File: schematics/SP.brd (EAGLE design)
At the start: 72.1 x 32 mm, 35 parts

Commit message: Поправлены платы МК, Радио, Гермо
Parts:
- removed BME280: BME280BME280-PINS-ONLY, UNKNOWN-2024:BME280-PINS-ONLY
- removed C2, C3, C4: 100nF, rcl:C0603
- removed JP2: (no value), pinhead:1X02
- removed MICS-5524: MICS_5524, UNKNOWN-2024:MICS-5524
- removed MICS-6814: MICS-6814, CanCubeSat:MICS-6814
- removed R11, R12, R13, R8: 10k, rcl:R0603
- removed R16, R17, R2: 5k1, rcl:R0603
- removed R39, R41, R43, R45: 100k, rcl:R0603
- removed R40, R42, R44, R46: 1M, rcl:R0603
- removed U$10, U$11, U$12, U$9: CONNECT_3, UNKNOWN-2024:CONNECT_3
- removed U$14: AD5593, UNKNOWN-2024:AD5593
- added C1: 47u, rcl:C1210
- added D1, D2, D3, D4, D5, D6, D7: MBR0520LT, diode:SOD123
- added FOTO: VT93N1VERT, KNPN-2023:VT93N1-VERT
- added PWR: (no value), led:CHIP-LED0603
- added SP-OUT: (no value), pinhead:1X02
- added U$1, U$3: SOLAR-2_1, KNPN-2023:SOLAR_1-2
- JP1: device pinhead:1X04 -> pinhead:1X02
- R1: value 5k1 -> 2k7
- U$2: value Плата ГЕРМО -> SOLAR-2_0; device UNKNOWN-2024:LOGO -> KNPN-2023:SOLAR_0-2
- U$4: value CCS811 -> SOLAR-2_0; device UNKNOWN-2024:CSS811 -> KNPN-2023:SOLAR_0-2
- U$5: value CONNECT_3 -> Плата СП; device UNKNOWN-2024:CONNECT_3 -> UNKNOWN-2024:LOGO
- U$6: value CONNECT_3 -> SOLAR-2_0; device UNKNOWN-2024:CONNECT_3 -> KNPN-2023:SOLAR_0-2
- U$7: value CONNECT_3 -> (none); device UNKNOWN-2024:CONNECT_3 -> KNPN-2023:VIAS-CONNECT
- U$8: value CONNECT_3 -> SOLAR-2_1; device UNKNOWN-2024:CONNECT_3 -> KNPN-2023:SOLAR_1-2
- moved U$6 71.4 mm to (8.00, -14.5), turned to 0 degrees
- moved U$8 70.9 mm to (7.50, -28.5), turned to 0 degrees
- moved U$5 69.6 mm to (0.00, -4.00)
- moved U$7 39.5 mm to (15.0, 4.20)
- moved JP1 37.2 mm to (15.0, 43.5), turned to 180 degrees
- moved U$2 16.8 mm to (7.20, 13.5), turned to 270 degrees
- moved R1 14.1 mm to (19.1, 38.1), flipped to the bottom, turned to 180 degrees
- moved U$4 5.01 mm to (22.8, 32.5), flipped to the top, turned to 90 degrees
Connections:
- removed net 3V3: C3.1, C4.1, R2.2, R40.1, R42.1, R44.1, R46.1, U$10.1, U$11.1, U$12.1, U$14.P$3, U$14.P$9, U$5.1, U$6.1, U$7.1, U$8.1, U$9.1
- removed net 5V: BME280.P$4, JP1.2, MICS-5524.P$4, MICS-6814.P$1, U$4.P$1
- removed net CO: MICS-6814.P$5, R8.2, U$14.P$7
- removed net EN: MICS-5524.P$1, R17.1
- removed net FOTO0: JP2.2, U$14.P$5
- removed net FOTO1: JP2.1, U$14.P$4
- removed net GND: BME280.P$3, C2.2, C3.2, C4.2, JP1.1, MICS-5524.P$3, MICS-6814.P$2, R1.2, R16.2, R17.2, U$14.P$14, U$4.P$2
- removed net MICS: MICS-5524.P$2, R13.2, U$14.P$11
- removed net N$10: R12.1, U$9.2
- removed net N$11: R44.2, U$10.3
- removed net N$12: R43.1, U$10.2
- removed net N$13: R45.2, U$11.3
- removed net N$14: R13.1, U$11.2
- removed net N$15: R46.2, U$12.3
- removed net N$16: R45.1, U$12.2
- removed net N$18: C2.1, U$14.P$8
- removed net N$19: R16.1, U$14.P$2
- removed net N$20: R2.1, U$14.P$1
- removed net N$5: R41.2, U$7.3
- removed net N$6: R11.1, U$7.2
- removed net N$7: R42.2, U$8.3
- removed net N$9: R43.2, U$9.3
- removed net NH3: MICS-6814.P$4, R12.2, U$14.P$6
- removed net NO2: MICS-6814.P$3, R11.2, U$14.P$10
- removed net SCL: BME280.P$2, JP1.4, U$14.P$16, U$4.P$3
- removed net SDA: BME280.P$1, JP1.3, U$14.P$15, U$4.P$4
- removed net WAC: R1.1, U$4.P$5
- new net SP+: C1.1, D1.A, D2.A, D5.A, D7.C, R1.1, U$1.IN-2, U$2.IN-2, U$6.IN-2
- new net SP+-: C1.2, D3.C, D4.C, D6.C, PWR.C, SP-OUT.1, U$3.OUT, U$4.OUT-2, U$4.OUT-21, U$7.1, U$8.OUT
- new net SP-: JP1.1, SP-OUT.2, U$7.2
- net N$1: now also D7.A, JP1.2; no longer R39.2, U$5.3
- net N$2: now also D2.C, D3.A, U$2.OUT-2, U$2.OUT-21, U$3.IN-2; no longer R8.1, U$5.2
- net N$3: now also D1.C, D4.A, U$1.OUT, U$4.IN-2; no longer R40.2, U$6.3
- net N$4: now also PWR.A, R1.2; no longer R39.1, U$6.2
- net N$8: now also D5.C, D6.A, U$6.OUT-2, U$6.OUT-21, U$8.IN-2; no longer R41.1, U$8.2
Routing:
- net GND: track 130.2 -> 0.00 mm
- net 3V3: track 118.0 -> 0.00 mm
- net 5V: track 87.2 -> 0.00 mm
- net SCL: track 70.8 -> 0.00 mm
- net SDA: track 55.5 -> 0.00 mm
- net SP+-: track 0.00 -> 43.5 mm
- net SP-: track 0.00 -> 43.1 mm
- net SP+: track 0.00 -> 38.2 mm, vias 0 -> 2
- net N$2: track 1.84 -> 23.3 mm, vias 0 -> 1
- net MICS: track 16.4 -> 0.00 mm
- net CO: track 13.8 -> 0.00 mm
- net N$3: track 1.84 -> 15.1 mm, vias 0 -> 1
- net FOTO0: track 13.1 -> 0.00 mm
- net FOTO1: track 10.2 -> 0.00 mm
- net NO2: track 9.75 -> 0.00 mm
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- added copper zone on layer 1, net SP-
- added copper zone on layer 16, net SP-
- removed copper zone on layer 1, net GND
- removed copper zone on layer 16, net GND
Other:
- board size 72.1 x 32 mm -> 30 x 46 mm
- board text added: "+"
- board text added: "-"
- board text added: "0.5V"
- board text added: "1.5V"
- board text added: "1V"
- board text added: "2V"
- board text added: "Solder on the last SP"
- board text added: "to Sat"

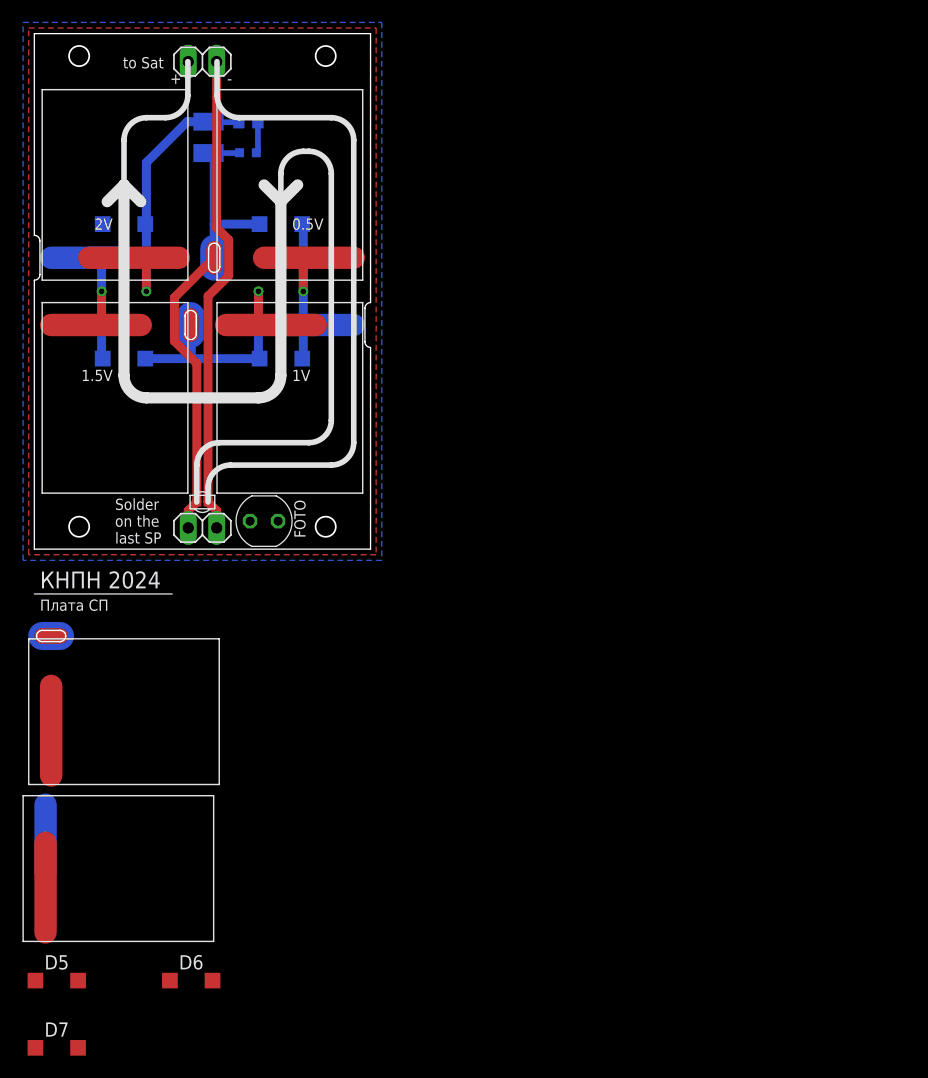
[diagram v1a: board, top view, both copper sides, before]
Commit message: схема платы моторов исправлена
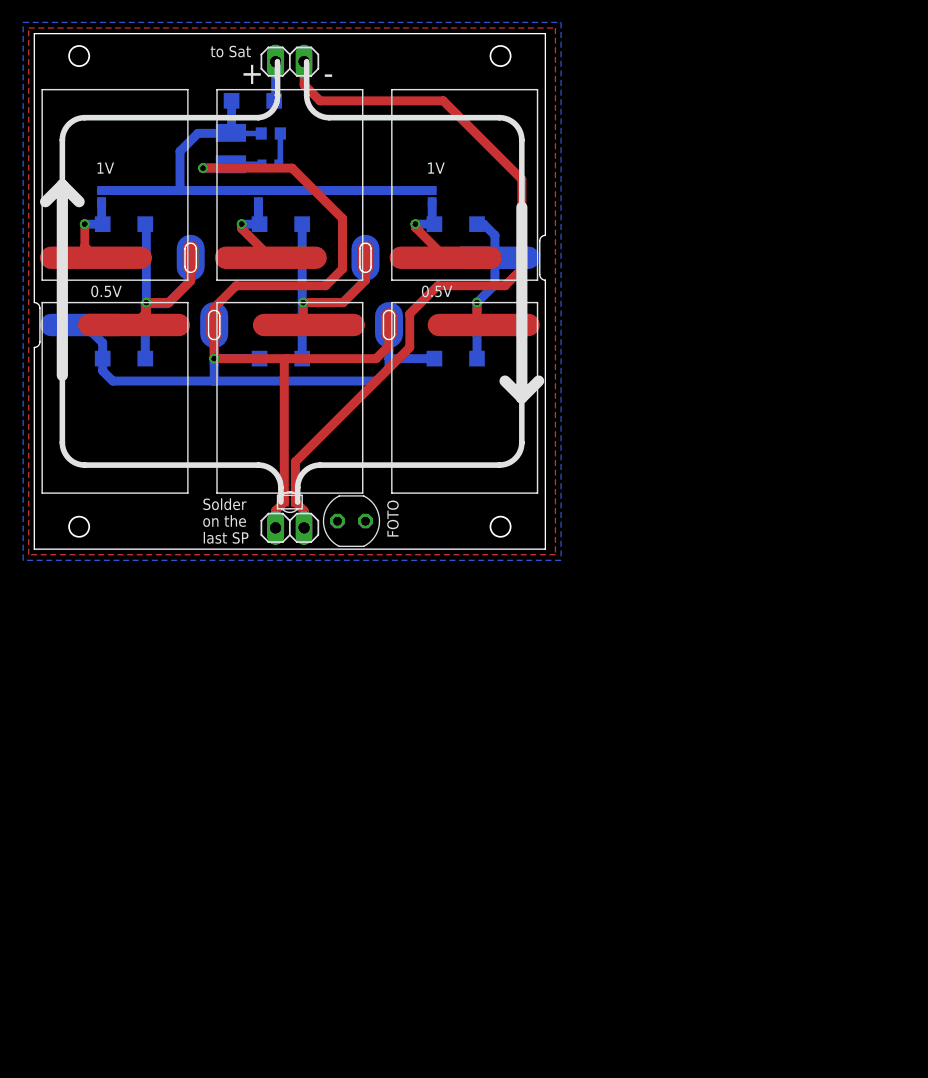
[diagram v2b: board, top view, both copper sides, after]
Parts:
- added U$10, U$11, U$9: (no value), KNPN-2023:VIAS-CONNECT
- U$1, U$3, U$8: value SOLAR-2_1 -> SOLAR-2_INVERT0-2; device KNPN-2023:SOLAR_1-2 -> KNPN-2023:SOLAR_0-2_INVERT
- U$2, U$6: value SOLAR-2_0 -> SOLAR-2_INVERT1-2; device KNPN-2023:SOLAR_0-2 -> KNPN-2023:SOLAR_1-2_INVERT
- U$4: value SOLAR-2_0 -> SOLAR-2_INVERT0-2; device KNPN-2023:SOLAR_0-2 -> KNPN-2023:SOLAR_0-2_INVERT
- moved D7 86.3 mm to (19.5, 40.0), flipped to the bottom, turned to 180 degrees
- moved D5 76.3 mm to (37.6, 29.0), flipped to the bottom
- moved D6 60.3 mm to (37.6, 17.0), flipped to the bottom, turned to 180 degrees
- moved U$6 56.0 mm to (38.4, 32.5), turned to 90 degrees
- moved U$8 52.1 mm to (38.4, 13.5), turned to 270 degrees
- moved U$5 32.4 mm to (29.0, 10.5), flipped to the bottom
- moved FOTO 7.80 mm to (28.3, 2.50)
- moved JP1 7.80 mm to (22.8, 43.5)
- moved SP-OUT 7.80 mm to (22.8, 1.90)
- moved U$7 7.80 mm to (22.8, 4.20)
- moved C1 2.24 mm to (17.5, 35.7)
- moved PWR 2.24 mm to (21.1, 34.4)
- moved R1 2.24 mm to (21.1, 37.1)
- turned D1 to 0 degrees
- turned D2 to 180 degrees
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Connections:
- new net N$5: D1.C, D2.A, U$1.OUT-2, U$1.OUT-21, U$2.IN-2
- new net N$6: D3.A, D4.C, U$3.IN-2, U$4.OUT-2, U$4.OUT-21
- new net N$7: D1.A, U$1.IN-2, U$9.1
- net N$2: now also D5.A, U$11.1, U$6.IN-2; no longer D2.C, D3.A, U$2.OUT-2, U$2.OUT-21, U$3.IN-2
- net N$3: now also U$10.1; no longer D1.C, U$1.OUT
- net N$8: now also U$6.OUT; no longer U$6.OUT-2, U$6.OUT-21
- net SP+: now also U$10.2, U$11.2, U$9.2; no longer D1.A, D2.A, D5.A, U$1.IN-2, U$2.IN-2, U$6.IN-2
- net SP+-: now also D2.C, U$2.OUT, U$3.OUT-2, U$3.OUT-21, U$8.OUT-2, U$8.OUT-21; no longer D4.C, U$3.OUT, U$4.OUT-2, U$4.OUT-21, U$8.OUT
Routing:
- net SP+-: track 43.5 -> 124.2 mm, vias 0 -> 2
- net N$6: track 0.00 -> 31.0 mm, vias 0 -> 1
- net N$5: track 0.00 -> 28.3 mm, vias 0 -> 1
- net SP-: track 43.1 -> 68.3 mm
- net N$8: track 0.00 -> 15.9 mm, vias 0 -> 1
- net N$2: track 23.3 -> 7.90 mm
- net N$3: track 15.1 -> 7.72 mm
- net N$7: track 0.00 -> 7.20 mm, vias 0 -> 1
- net SP+: track 38.2 -> 43.9 mm, vias 2 -> 0
- net N$1: track 0.00 -> 3.55 mm
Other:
- board size 30 x 46 mm -> 45.6 x 46 mm
- board text removed: "1.5V"
- board text removed: "2V"

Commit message: проверка плат
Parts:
- moved U$5 12.1 mm to (18.5, 4.50)
- moved U$9 2.00 mm to (4.00, 31.5)
- moved U$10 1.50 mm to (18.5, 31.5)
- moved U$11 1.50 mm to (34.0, 31.5)
- moved R1 0.50 mm to (21.1, 37.6)
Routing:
- net SP+: track 43.9 -> 44.6 mm
- net N$4: track 2.78 -> 3.28 mm
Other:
- board text added: "0V"
